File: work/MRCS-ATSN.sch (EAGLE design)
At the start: 63 parts, among them IC1 LM324N, IC2 LM324N, J1 RJ14, J2 RJ14, Q1 2N4401, Q2 2N4403, T1 TY-145P

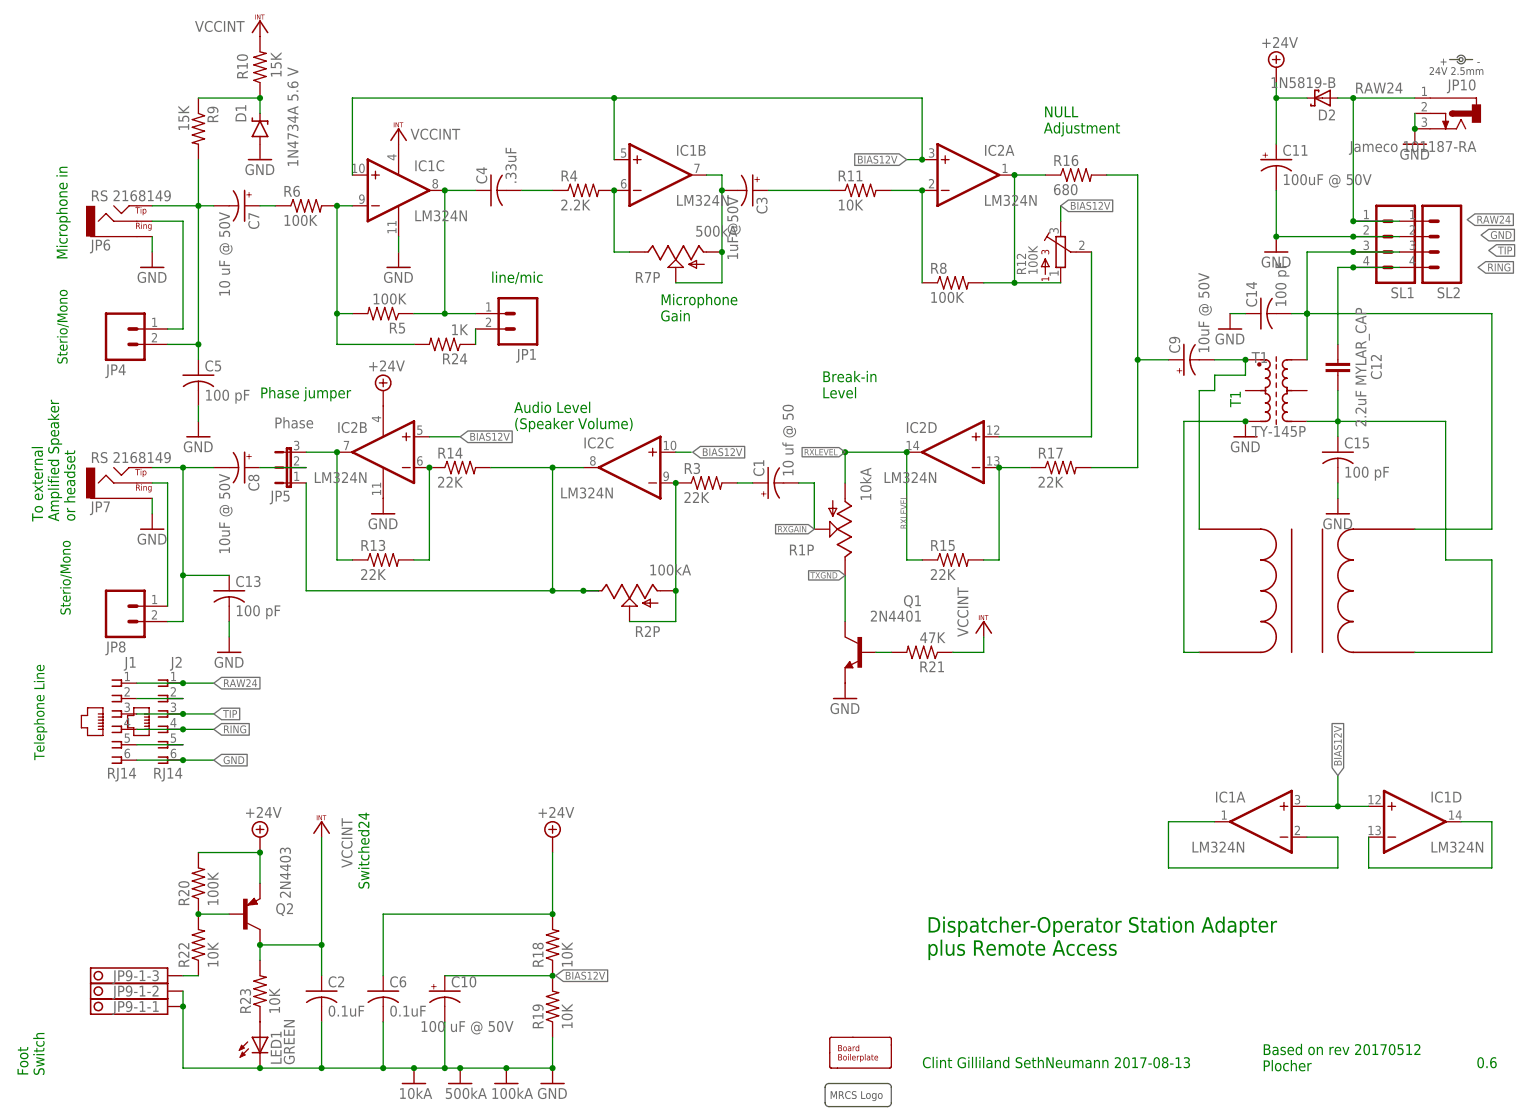
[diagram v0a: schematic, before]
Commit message: clean up of messy import
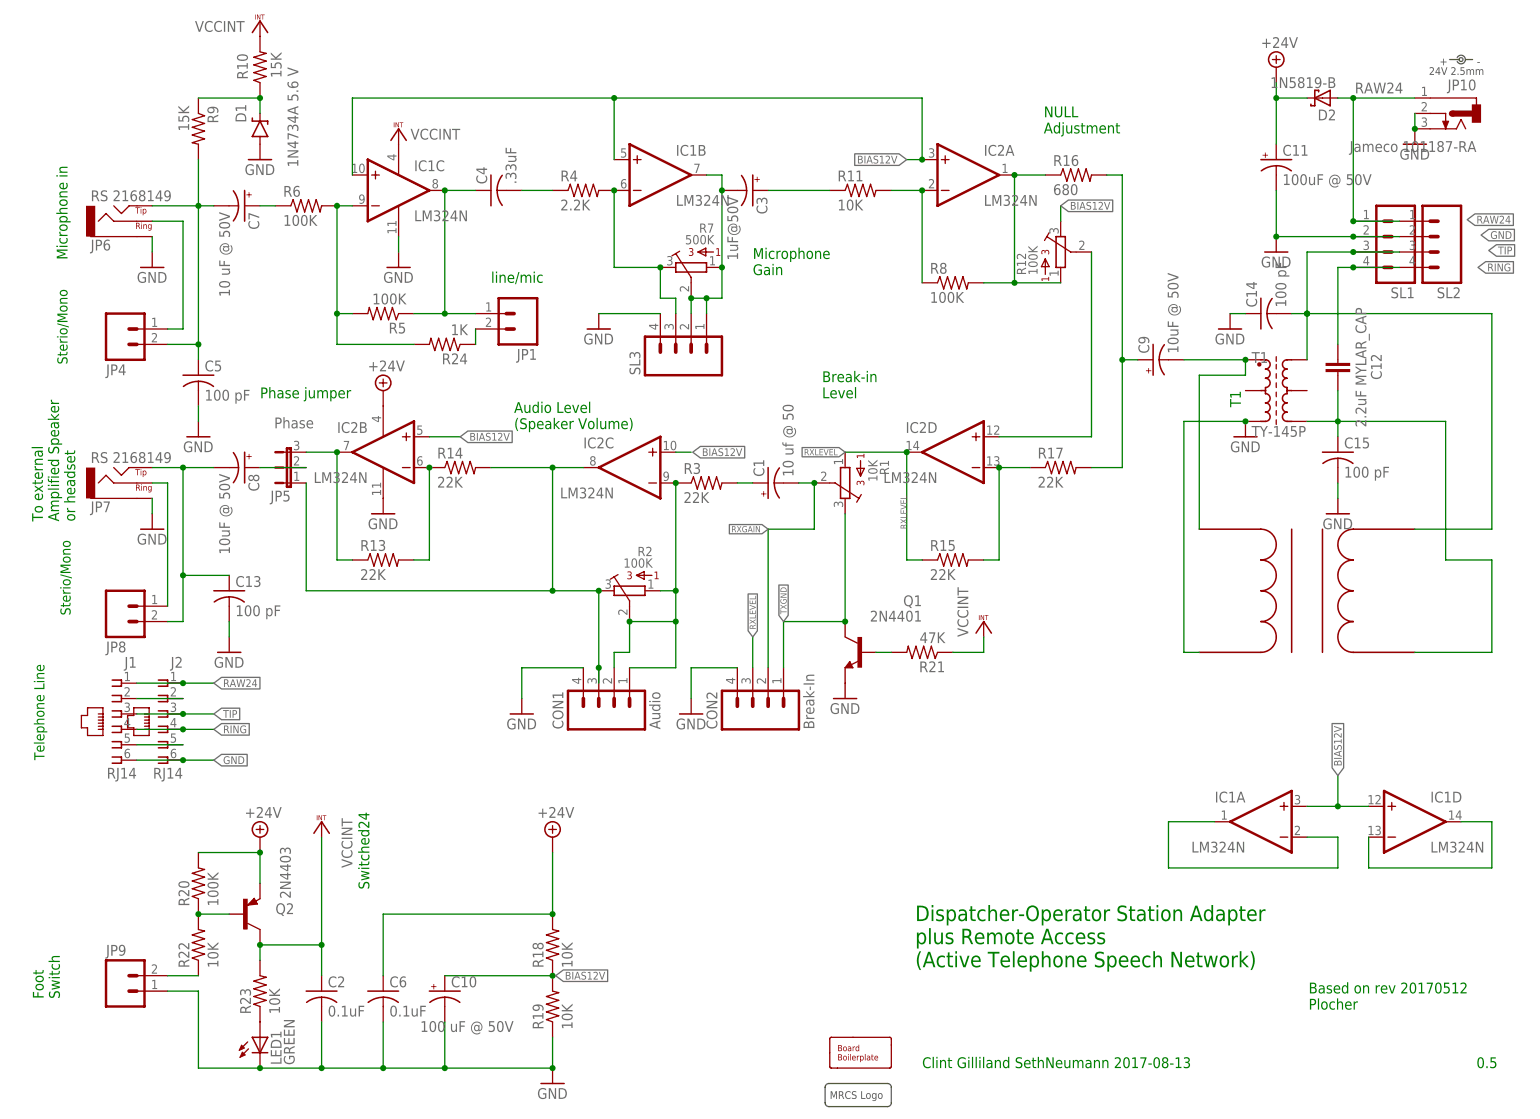
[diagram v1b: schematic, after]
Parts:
- removed JP9-1: 1751251, con-phoenix-350:1751251
- added CON1: Audio, SPCoast 2017_04:CONNECTOR-M04LOCK
- added CON2: Break-In, SPCoast 2017_04:CONNECTOR-M04LOCK
- added JP9: (no value), SPCoast:CONNECTOR-M02508-LOCK
- added SL3: (no value), SPCoast:CONNECTOR-M04POLAR_LOCK
- R1: value 10kA -> 10K; device SPCoast:R-POT-MRCS -> bourns_test:3386-K
- R2: value 100kA -> 100K; device SPCoast:R-POT-MRCS -> bourns_test:3386-K
- R7: value 500kA -> 500K; device SPCoast:R-POT-MRCS -> bourns_test:3386-K
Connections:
- removed net N$9: JP9-1-3.K, R22.1
- new net N$16: JP9.2, R22.1
- net GND: now also CON1.4, CON2.4, JP9.1, SL3.4; no longer JP9-1-1.K, JP9-1-2.K, R1GND.GND, R2GND.GND, R7GND.GND
- net N$13: now also R7.1, R7.2, SL3.1, SL3.2; no longer R7P.A, R7P.S
- net N$20: now also CON1.1, CON1.2, R2.1, R2.2; no longer R2P.A, R2P.S
- net N$38: now also R7.3, SL3.3; no longer R7P.E
- net N$40: now also CON1.3, R2.3; no longer R2P.E
- net RXGAIN: now also CON2.2, R1.2; no longer R1P.S
- net RXLEVEL: now also CON2.3, R1.1; no longer R1P.A
- net TXGND: now also CON2.1, R1.3; no longer R1P.E
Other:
- note added: "-unused-"
- note added: "0.5"
- note added: "Dispatcher-Operator Station Adapter plus Remote Access (Active Telephone Speech Network)"
- note removed: "0.6"
- note removed: "Dispatcher-Operator Station Adapter plus Remote Access"
- moved on the sheet: C9
